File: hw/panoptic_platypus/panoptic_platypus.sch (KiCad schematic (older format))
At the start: 34 parts

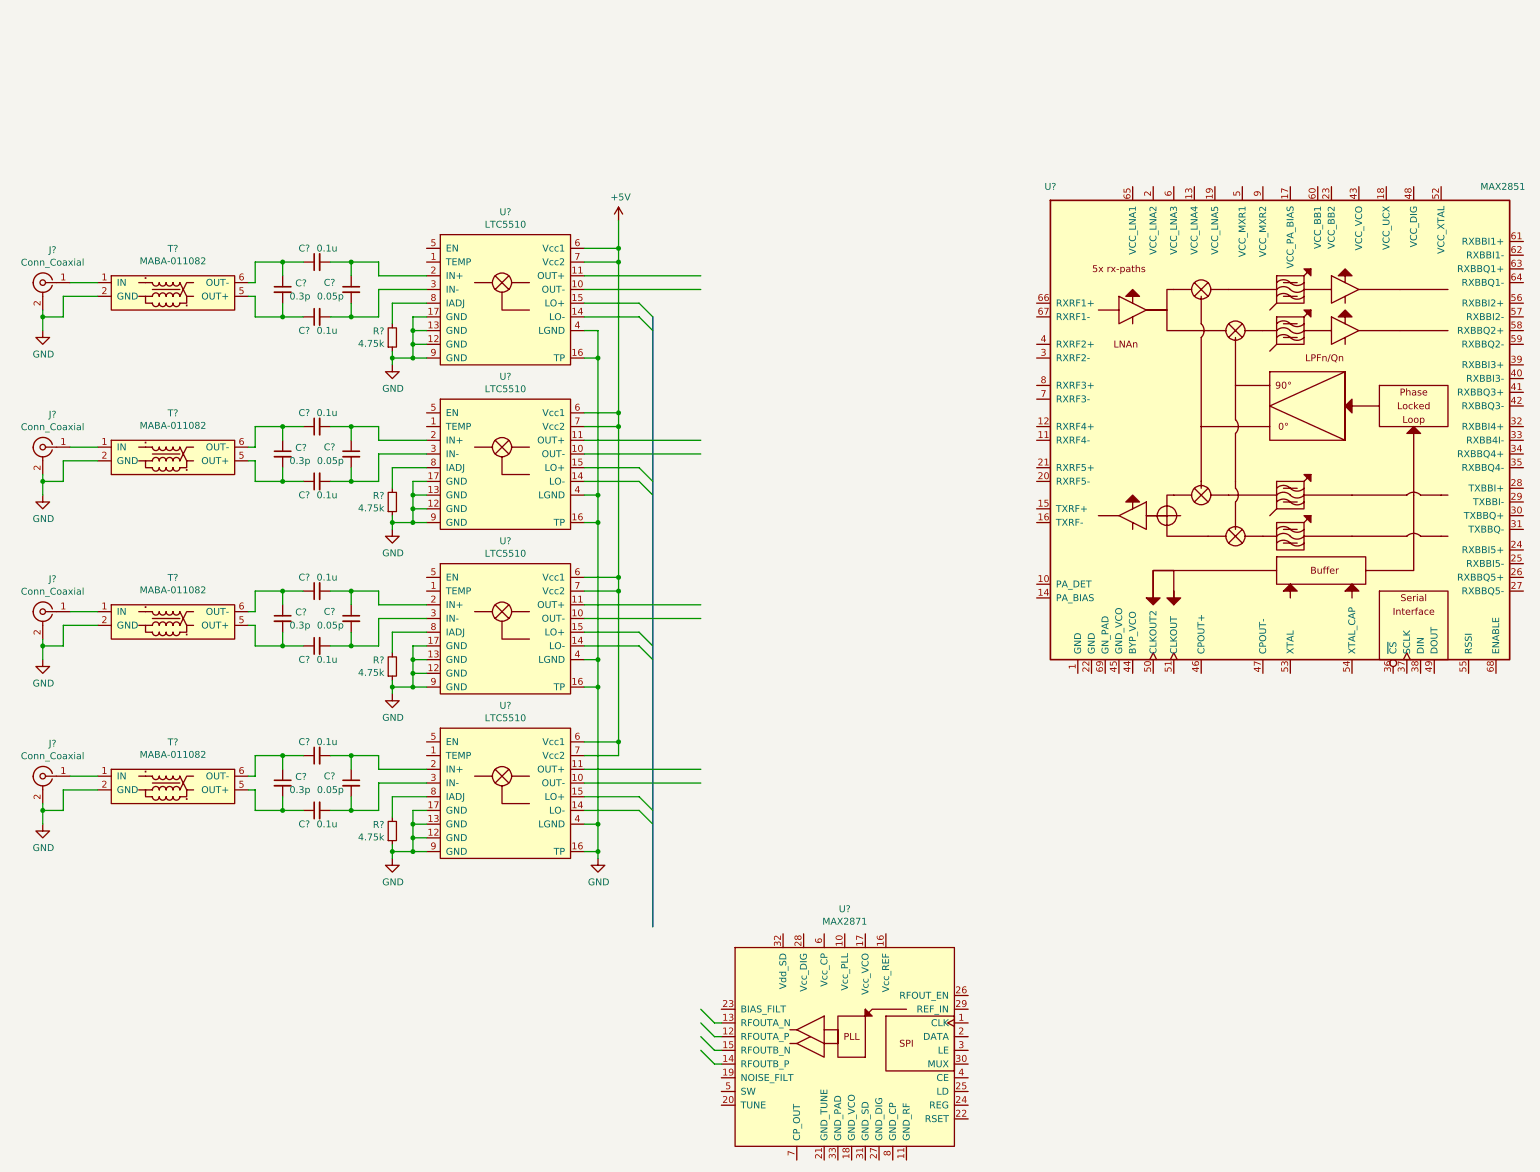
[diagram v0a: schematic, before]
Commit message: changed input stage to be hierachial
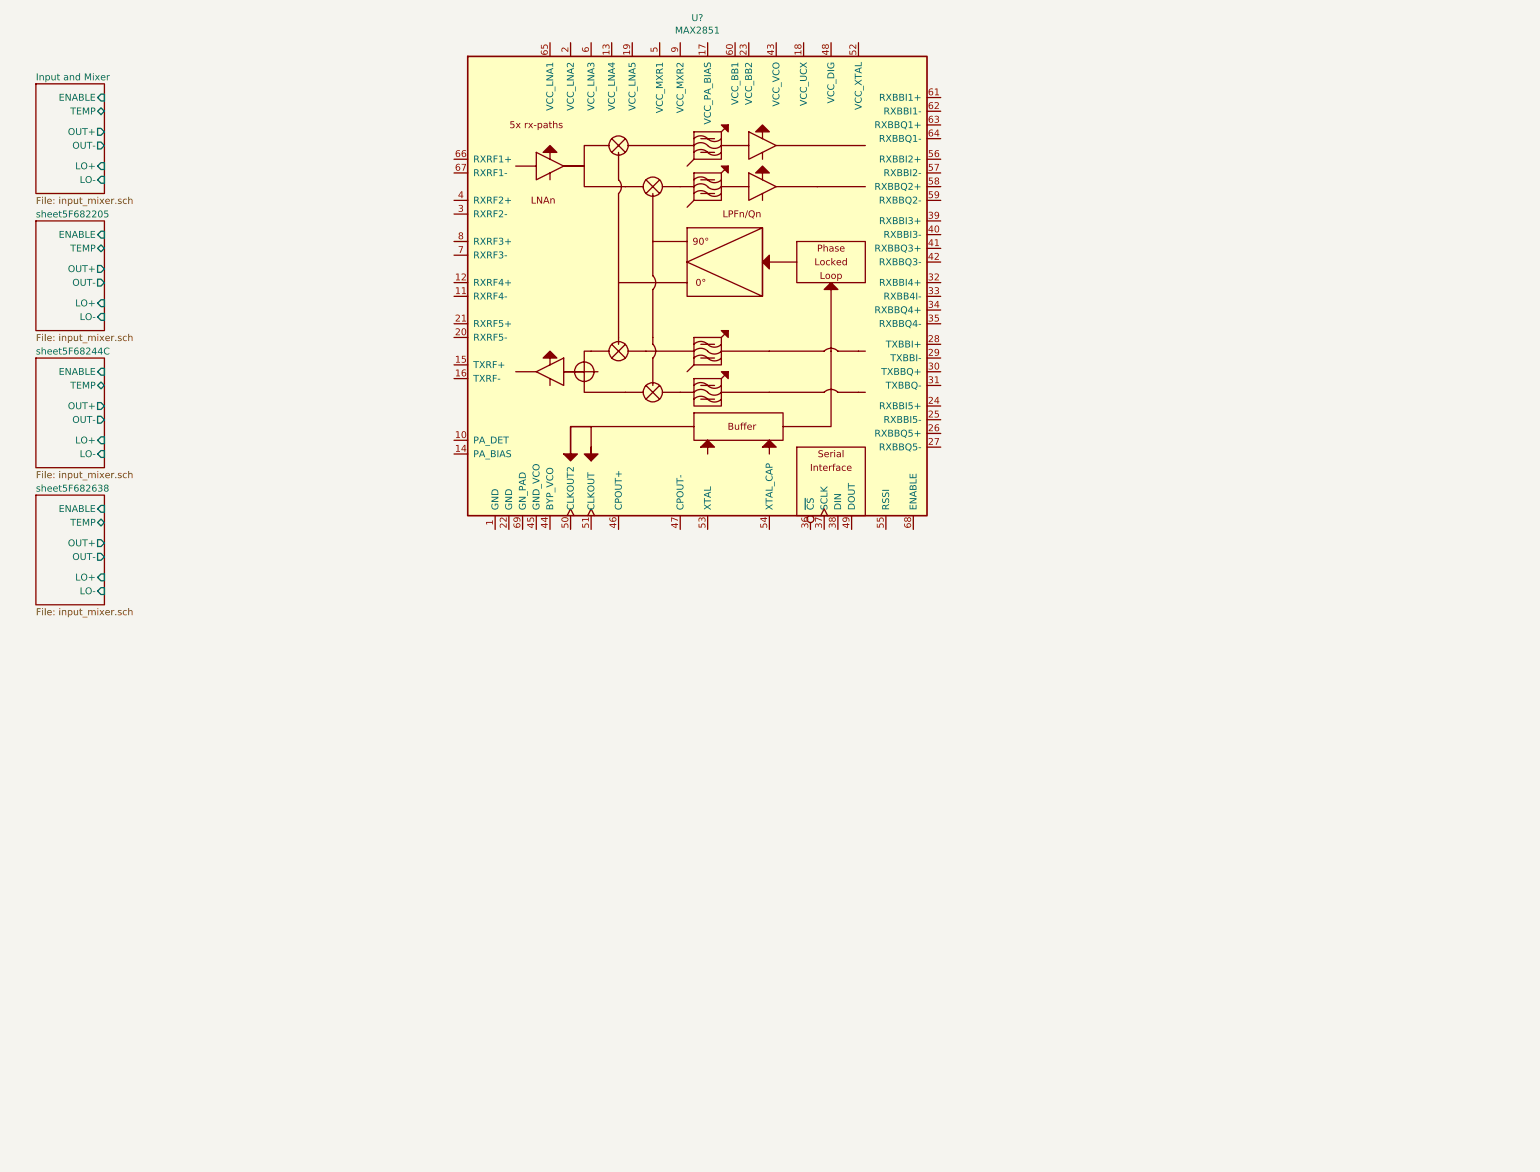
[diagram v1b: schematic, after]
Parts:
- removed C? (x4): 0.3p, symbol Device:C_Small
- removed C? (x8): 0.1u, symbol Device:C_Small
- removed C? (x4): 0.05p, symbol Device:C_Small
- removed J? (x4): Conn_Coaxial, symbol Connector:Conn_Coaxial
- removed R? (x4): 4.75k, symbol Device:R_Small
- removed T? (x4): MABA-011082, symbol dknueppe_symbols:MABA-011082
- removed U?: MAX2851, symbol dknueppe_symbols:MAX2851
- removed U? (x4): LTC5510, Package_DFN_QFN:QFN-16-1EP_5x5mm_P0.8mm_EP2.7x2.7mm_ThermalVias, symbol dknueppe_symbols:LTC5510
- removed U?: MAX2871, symbol dknueppe_symbols:MAX2871
- added U?: MAX2851, symbol dknueppe_symbols:MAX2851
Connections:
- net labels removed: +5V, GND
- wire segments 204 -> 0

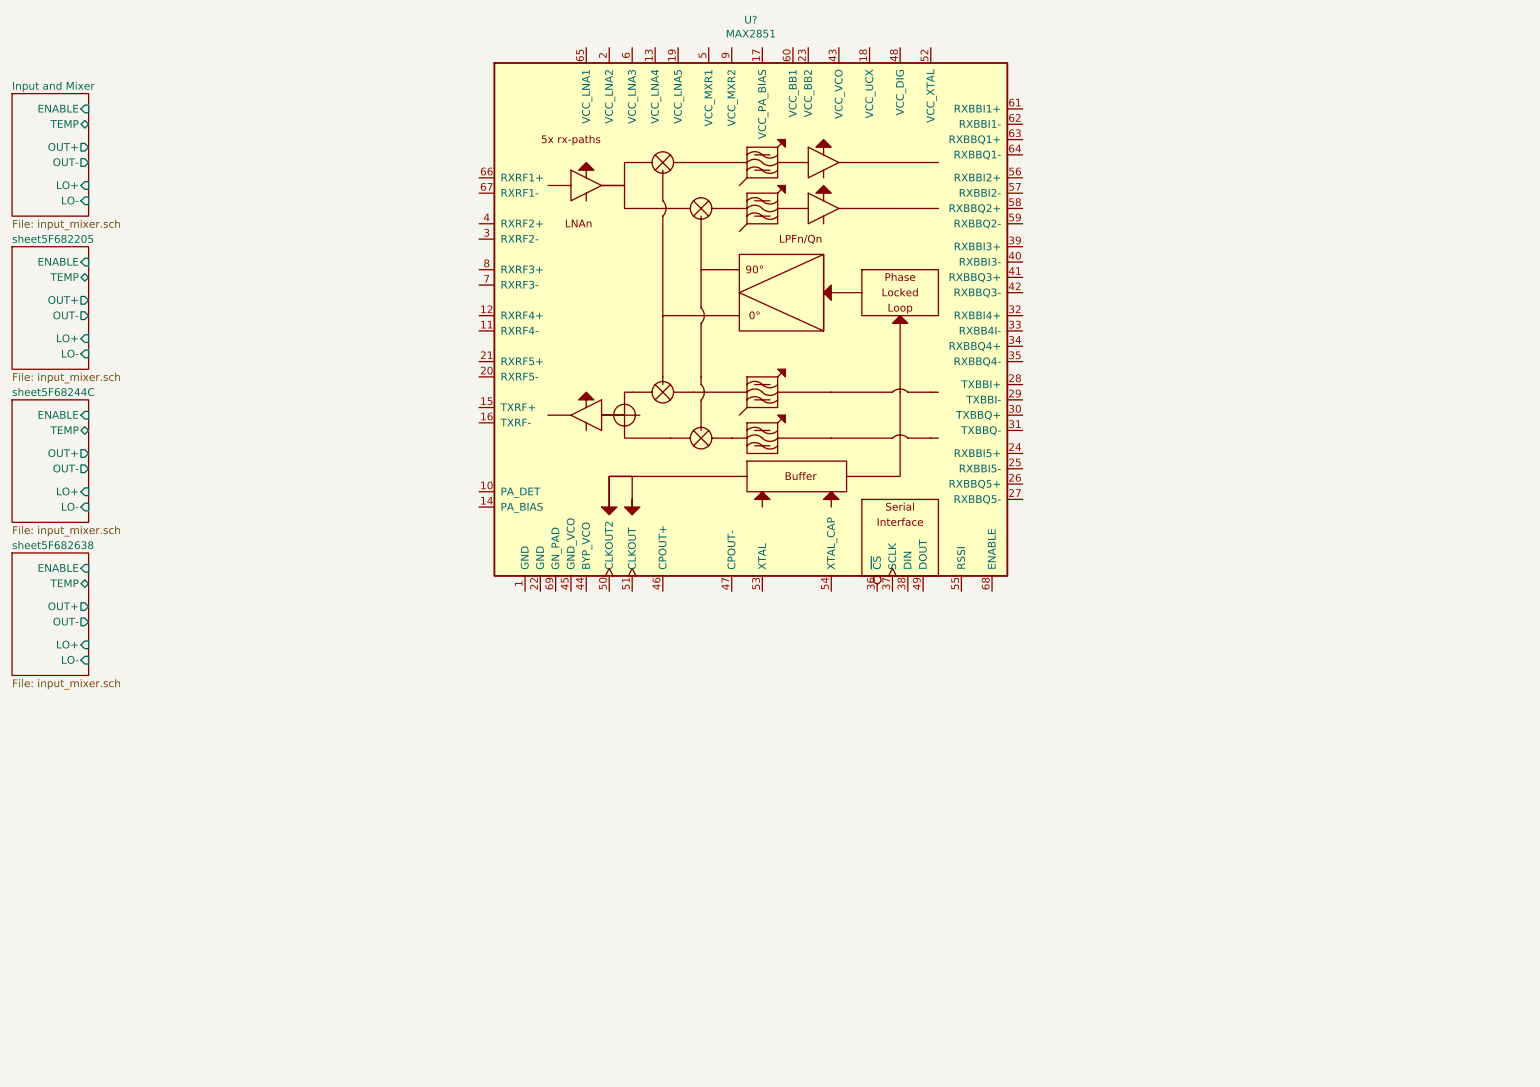
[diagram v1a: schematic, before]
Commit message: Added ADC decoupling and input filter
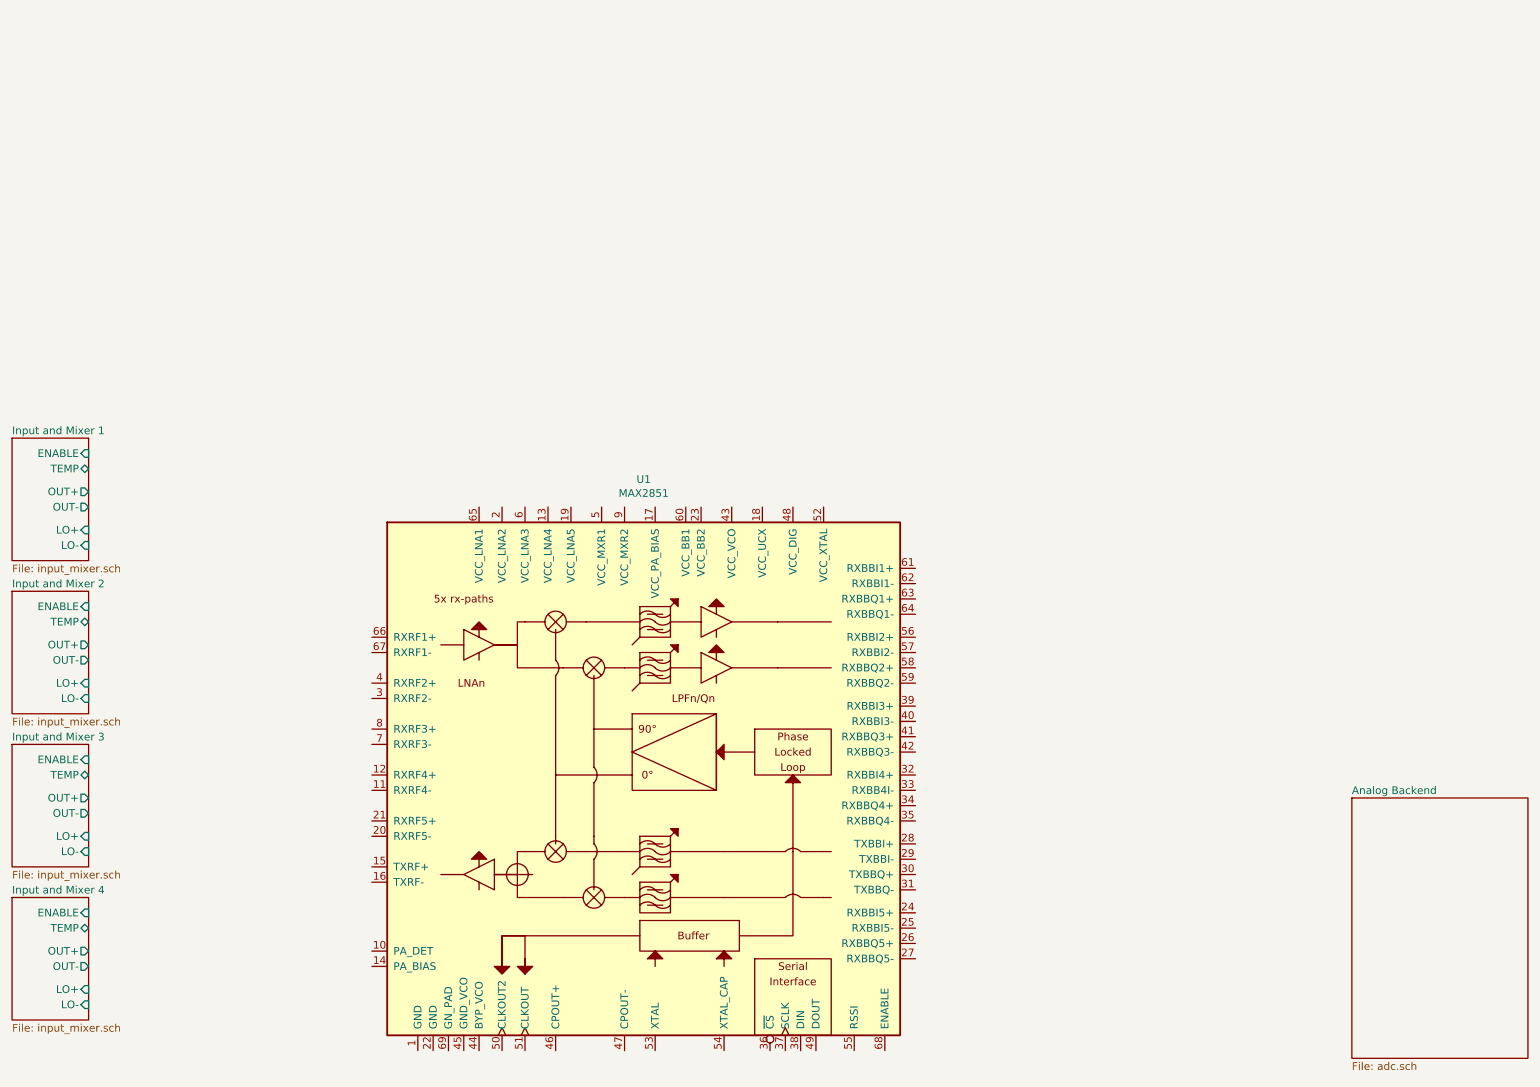
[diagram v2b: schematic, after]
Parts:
- gave numbers to parts that had none: 1
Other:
- moved on the sheet: U1
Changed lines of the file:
@@
 EELAYER 30 0
 EELAYER END
-$Descr A4 11693 8268
+$Descr A3 16535 11693
 encoding utf-8
-Sheet 1 2
-Title ""
-Date ""
-Rev ""
+Sheet 1 6
+Title "Panoptic Platypus"
+Date "2020-09-21"
+Rev "revA0"
 Comp ""
 Comment1 ""
@@
 $EndDescr
 $Comp
-L dknueppe_symbols:MAX2851 U?
+L dknueppe_symbols:MAX2851 U1
 U 1 1 5F68B4A5
-P 5800 2500
-F 0 "U?" H 5775 4581 50  0000 C CNN
-F 1 "MAX2851" H 5775 4490 50  0000 C CNN
-F 2 "" H 4100 800 50  0000 C CNN
-F 3 "" H 4100 800 50  0001 C CNN
-	1    5800 2500
+P 5100 5500
+F 0 "U1" H 5075 7581 50  0000 C CNN
+F 1 "MAX2851" H 5075 7490 50  0000 C CNN
+F 2 "" H 3400 3800 50  0000 C CNN
+F 3 "" H 3400 3800 50  0001 C CNN
+	1    5100 5500
 	1    0    0    -1
 $EndComp
 $Sheet
-S 950  900  500  800
+S 950  3150 500  800
 U 5F68A5E9
-F0 "Input and Mixer" 50
+F0 "Input and Mixer 1" 50
 F1 "input_mixer.sch" 50
-F2 "LO+" I R 1450 1500 50
-F3 "LO-" I R 1450 1600 50
-F4 "OUT+" O R 1450 1250 50
-F5 "OUT-" O R 1450 1350 50
-F6 "ENABLE" I R 1450 1000 50
-F7 "TEMP" B R 1450 1100 50
+F2 "LO+" I R 1450 3750 50
+F3 "LO-" I R 1450 3850 50
+F4 "OUT+" O R 1450 3500 50
+F5 "OUT-" O R 1450 3600 50
+F6 "ENABLE" I R 1450 3250 50
+F7 "TEMP" B R 1450 3350 50
 $EndSheet
 $Sheet
-S 950  1900 500  800
+S 950  4150 500  800
 U 5F68220D
-F0 "sheet5F682205" 50
+F0 "Input and Mixer 2" 50
 F1 "input_mixer.sch" 50
-F2 "LO+" I R 1450 2500 50
-F3 "LO-" I R 1450 2600 50
-F4 "OUT+" O R 1450 2250 50
-F5 "OUT-" O R 1450 2350 50
-F6 "ENABLE" I R 1450 2000 50
-F7 "TEMP" B R 1450 2100 50
+F2 "LO+" I R 1450 4750 50
+F3 "LO-" I R 1450 4850 50
+F4 "OUT+" O R 1450 4500 50
+F5 "OUT-" O R 1450 4600 50
+F6 "ENABLE" I R 1450 4250 50
+F7 "TEMP" B R 1450 4350 50
 $EndSheet
 $Sheet
-S 950  2900 500  800
+S 950  5150 500  800
 U 5F682454
-F0 "sheet5F68244C" 50
+F0 "Input and Mixer 3" 50
 F1 "input_mixer.sch" 50
-F2 "LO+" I R 1450 3500 50
-F3 "LO-" I R 1450 3600 50
-F4 "OUT+" O R 1450 3250 50
-F5 "OUT-" O R 1450 3350 50
-F6 "ENABLE" I R 1450 3000 50
-F7 "TEMP" B R 1450 3100 50
+F2 "LO+" I R 1450 5750 50
+F3 "LO-" I R 1450 5850 50
+F4 "OUT+" O R 1450 5500 50
+F5 "OUT-" O R 1450 5600 50
+F6 "ENABLE" I R 1450 5250 50
+F7 "TEMP" B R 1450 5350 50
 $EndSheet
 $Sheet
-S 950  3900 500  800
+S 950  6150 500  800
 U 5F682640
-F0 "sheet5F682638" 50
+F0 "Input and Mixer 4" 50
 F1 "input_mixer.sch" 50
-F2 "LO+" I R 1450 4500 50
-F3 "LO-" I R 1450 4600 50
-F4 "OUT+" O R 1450 4250 50
-F5 "OUT-" O R 1450 4350 50
-F6 "ENABLE" I R 1450 4000 50
-F7 "TEMP" B R 1450 4100 50
+F2 "LO+" I R 1450 6750 50
+F3 "LO-" I R 1450 6850 50
+F4 "OUT+" O R 1450 6500 50
+F5 "OUT-" O R 1450 6600 50
+F6 "ENABLE" I R 1450 6250 50
+F7 "TEMP" B R 1450 6350 50
+$EndSheet
+$Sheet
+S 9700 5500 1150 1700
+U 5F6B2AD8
+F0 "Analog Backend" 50
+F1 "adc.sch" 50
 $EndSheet
 $EndSCHEMATC
